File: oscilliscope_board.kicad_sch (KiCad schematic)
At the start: 34 parts, among them J1 Conn_Coaxial, J2 Conn_Coaxial, SW1 SW_Push, SW2 RotaryEncoder_Switch_MP, U2 ADC0832

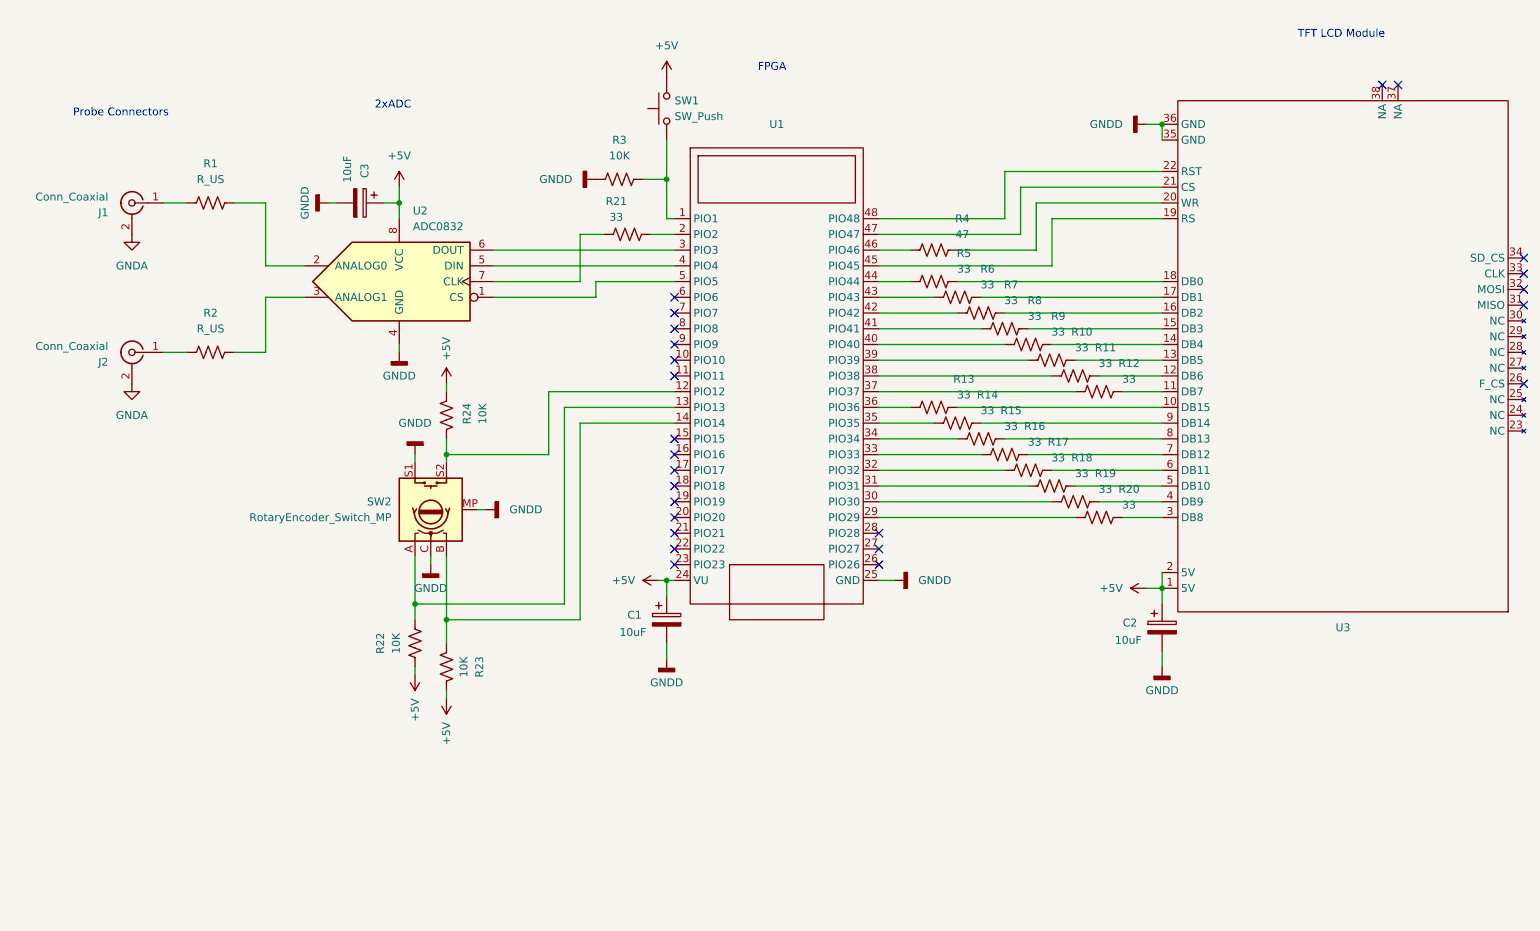
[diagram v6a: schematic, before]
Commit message: routed all board connections. needs review
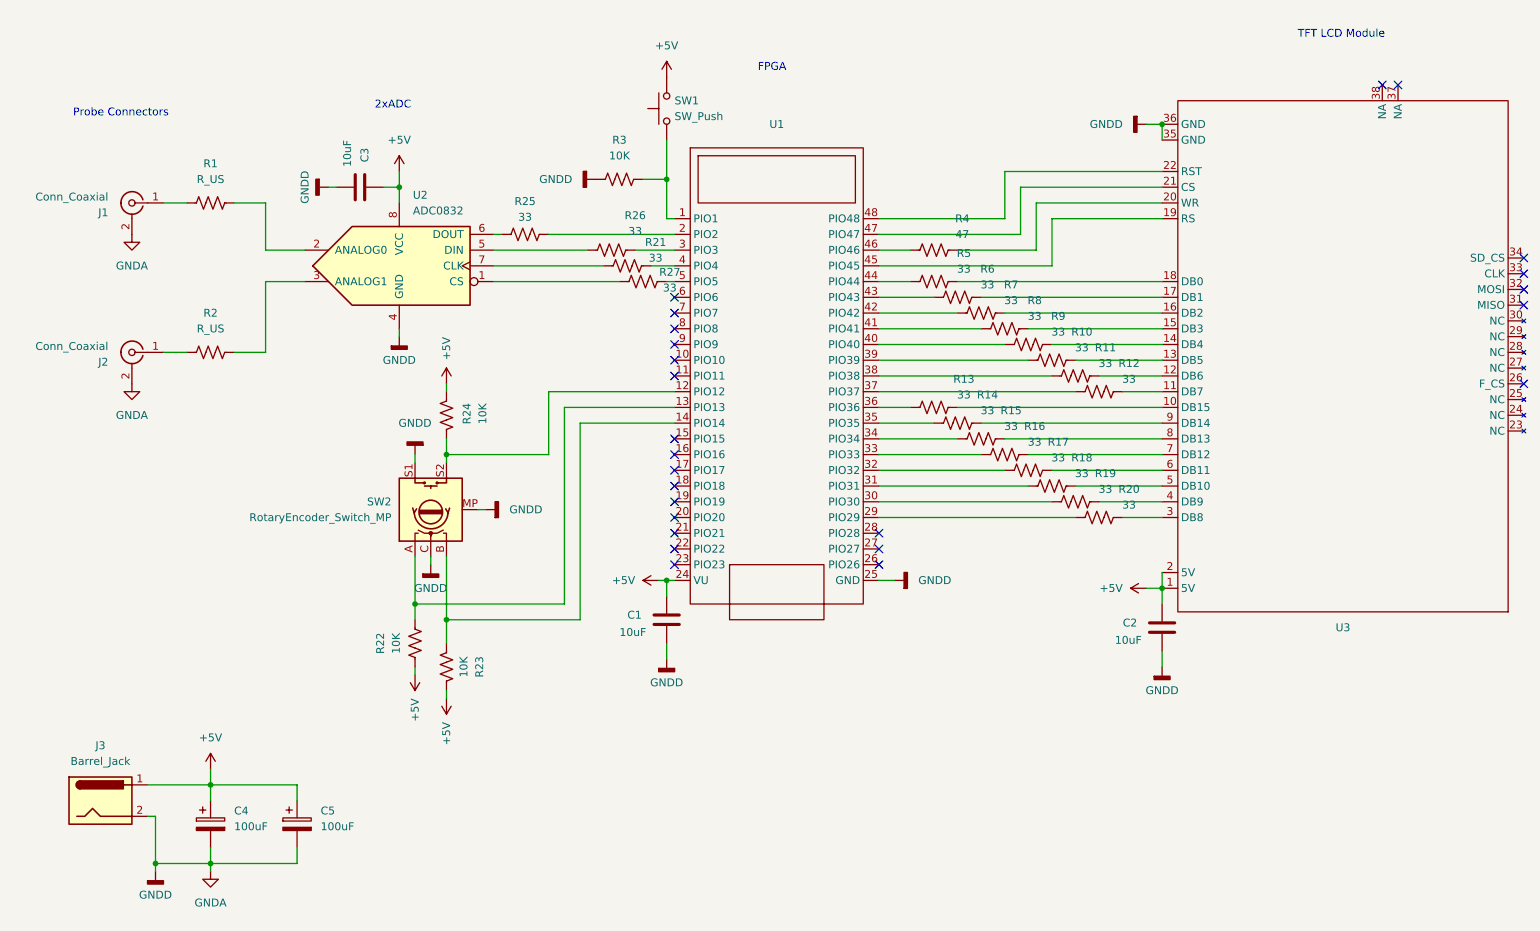
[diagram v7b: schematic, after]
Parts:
- added C4, C5: 100uF, Capacitor_THT:CP_Radial_D8.0mm_P2.50mm, symbol Device:C_Polarized
- added J3: Barrel_Jack, Connector_BarrelJack:BarrelJack_GCT_DCJ200-10-A_Horizontal, symbol Connector:Barrel_Jack
- added R25, R26, R27: 33, Resistor_SMD:R_0805_2012Metric_Pad1.20x1.40mm_HandSolder, symbol Device:R_US
- C1, C2, C3: footprint Capacitor_THT:CP_Radial_D8.0mm_P5.00mm -> Capacitor_THT:C_Disc_D4.7mm_W2.5mm_P5.00mm; symbol Device:C_Polarized -> Device:C
- R1, R10, R11, R12, R13, R14, R15, R16, R17, R18, R19, R2, R20, R21, R22, R23, R24, R4, R5, R6, R7, R8, R9: footprint Resistor_SMD:R_1206_3216Metric_Pad1.30x1.75mm_HandSolder -> Resistor_SMD:R_0805_2012Metric_Pad1.20x1.40mm_HandSolder
- R3: footprint Resistor_THT:R_Axial_DIN0204_L3.6mm_D1.6mm_P7.62mm_Horizontal -> Resistor_SMD:R_1206_3216Metric_Pad1.30x1.75mm_HandSolder
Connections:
- net GNDD is gone; now on net GNDA: C1.2, C2.2, C3.2, R3.1, SW2.C, SW2.MP, SW2.S1, U1.25 (GND), U2.4 (GND), U3.35 (GND), U3.36 (GND)
- net +5V: now also C4.1, C5.1, J3.1
- net GNDA: now also C4.2, C5.2, J3.2
- net at U1.2 (PIO2): now also R25.2; no longer R21.2
- net at U2.1 (CS): now also R27.1; no longer U1.5 (PIO5)
- net at U1.4 (PIO4): now also R21.2; no longer U2.5 (DIN)
- net at U2.6 (DOUT): now also R25.1; no longer U1.3 (PIO3)
- new net: R26.1, U2.5 (DIN)
- new net: R26.2, U1.3 (PIO3)
- new net: R27.2, U1.5 (PIO5)
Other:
- moved on the sheet: R21, U2

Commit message: added mounting holes for stand-off legs
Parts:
- added H1, H2, H3, H4: MountingHole_Pad, MountingHole:MountingHole_3.2mm_M3_DIN965_Pad, symbol Mechanical:MountingHole_Pad
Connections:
- net GNDA renamed GNDD
- net GNDD: now also H1.1, H2.1, H3.1, H4.1
